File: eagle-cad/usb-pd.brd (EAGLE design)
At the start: 100 x 80 mm, 24 parts, among them Q1 CERAMIC_RESONATOR_SMD6M00G53Z, U1 ATMEGA328-AU

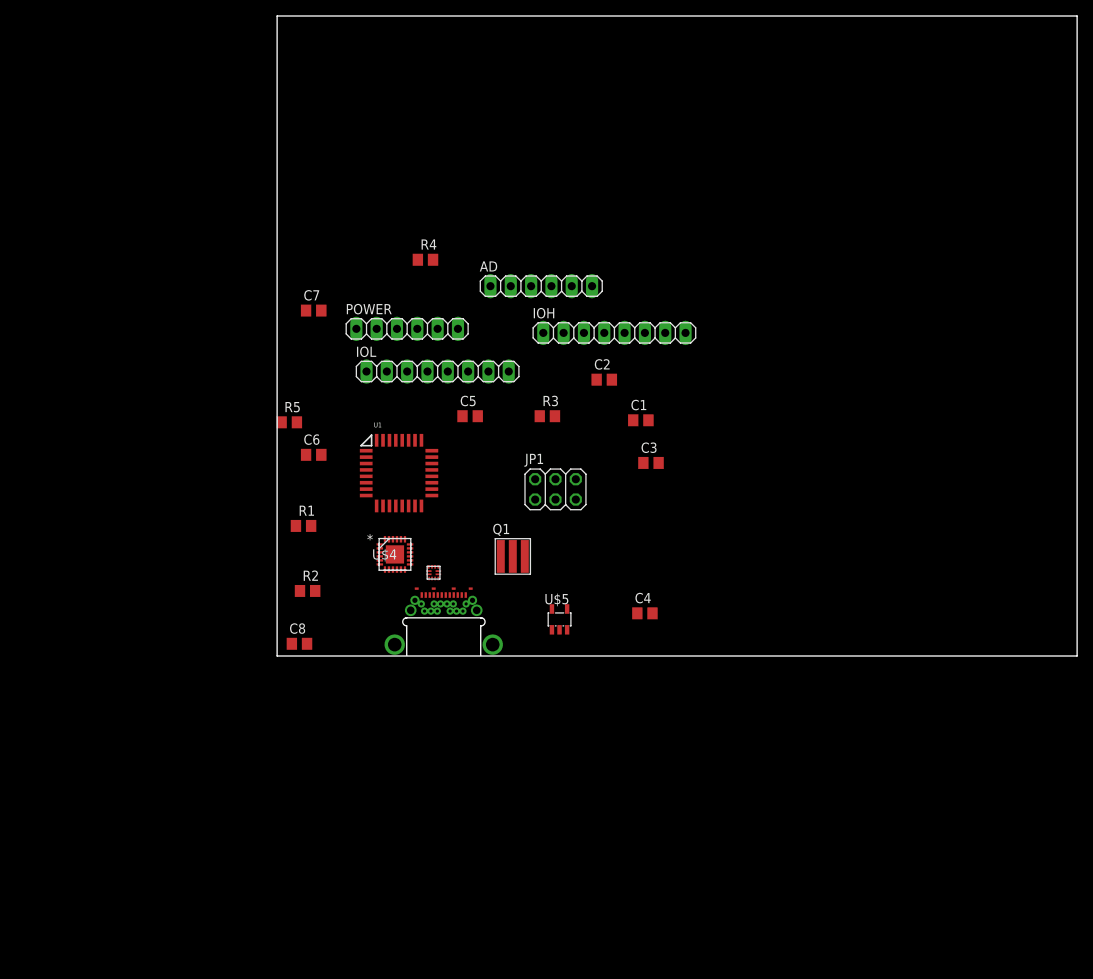
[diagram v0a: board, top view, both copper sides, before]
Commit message: Filled out PTN5150, arranged board like an Uno rev3
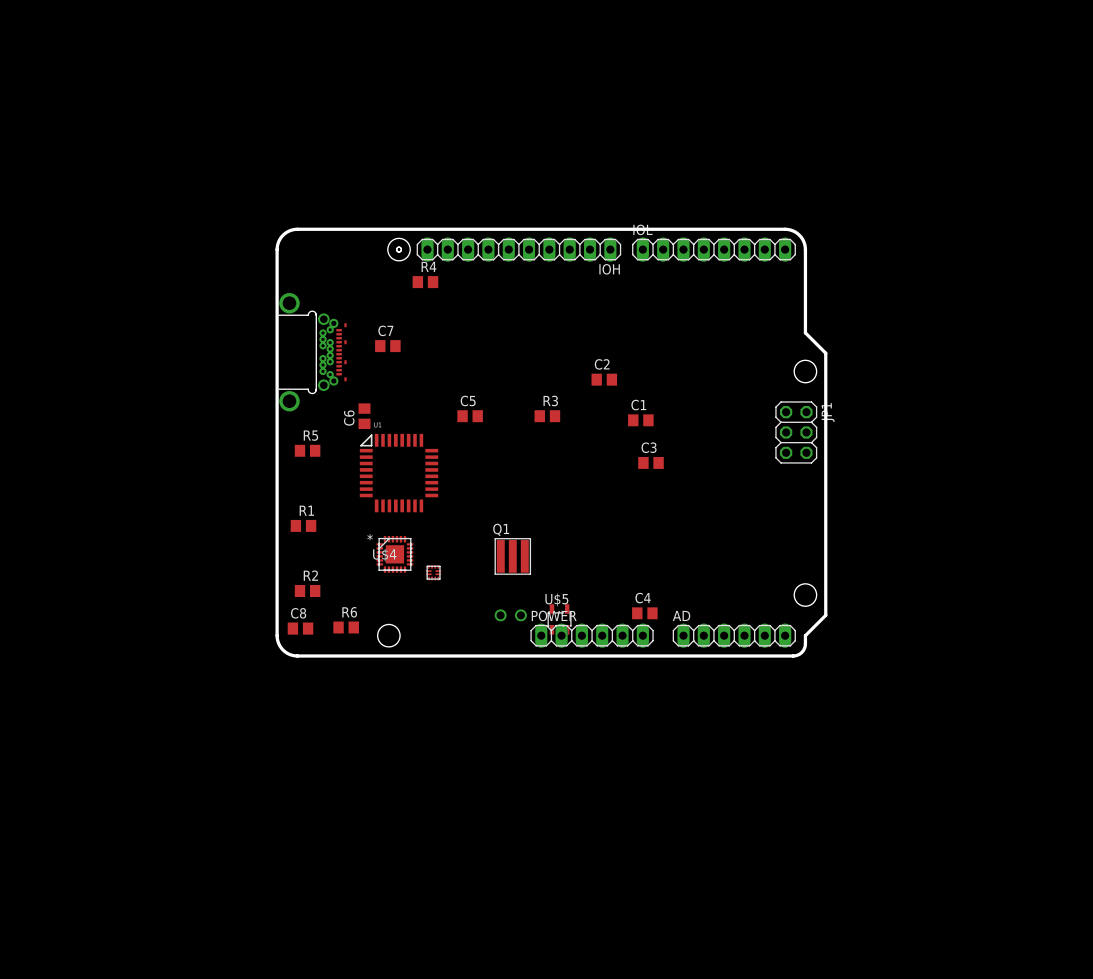
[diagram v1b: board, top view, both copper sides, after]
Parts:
- added R6: 10k, rcl:R0805
- IOH: device pinhead:1X08 -> pinhead:1X10
- R3: value (none) -> 10k
- moved AD 49.9 mm to (57.1, 2.54)
- moved POWER 44.8 mm to (39.4, 2.54)
- moved IOL 37.8 mm to (54.6, 50.8)
- moved U$1 33.1 mm to (7.75, 38.0), turned to 270 degrees
- moved JP1 30.9 mm to (64.9, 27.9), turned to 270 degrees
- moved IOH 15.8 mm to (30.2, 50.8), turned to 180 degrees
- moved C7 10.3 mm to (13.8, 38.7)
- moved C6 7.98 mm to (10.9, 30.0), turned to 90 degrees
- moved R5 4.23 mm to (3.81, 25.7)
- moved R4 2.79 mm to (18.5, 46.7)
- moved C8 1.91 mm to (2.92, 3.43)
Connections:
- new net N$8: R6.1, U$3.P$5
- net +5V: now also R6.2, U$3.P$12
- net GND: now also U$1.A$1, U$1.A$12, U$1.B$1, U$1.B$12, U$3.P$10, U$3.P$11, U$3.P$3
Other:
- board size 100 x 80 mm -> 68.6 x 53.3 mm

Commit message: Added 5V buck implementation (need power FET to control it)
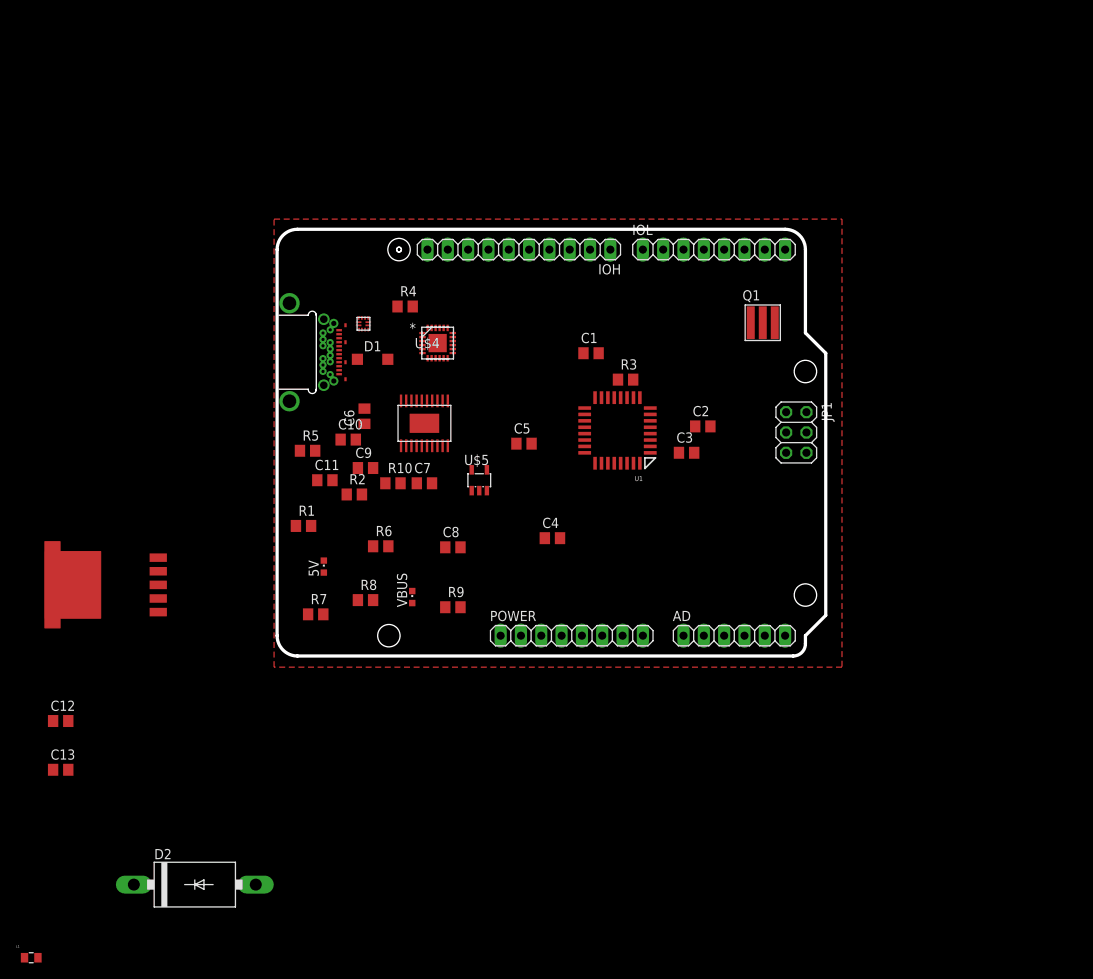
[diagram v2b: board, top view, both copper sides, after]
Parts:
- added 5V, VBUS: (no value), led:CHIPLED_0603
- added C10, C11: 47uF, rcl:C0805
- added C12: 100uF, rcl:C0805
- added C13: 1mF, rcl:C0805
- added C9: (no value), rcl:C0805
- added D1: MBR0520LT, diode:SOD123
- added D2: 1N5822, diode:DO201-15
- added L1: (no value), EagleLibrary_Wuerth_Elektronik_eiSos_rev16a:WE-RFI_0805
- added R10: 10k, rcl:R0805
- added R7: 300, rcl:R0805
- added R8, R9: 1.5k, rcl:R0805
- added U$2: TI-TPS7B6750-Q1, usb-pd:HTSSOP-20
- added U$6: TI-LM2576-5.0, usb-pd:TO-263
- POWER: device pinhead:1X06 -> pinhead:1X08
- moved Q1 42.8 mm to (60.7, 41.7)
- moved U$3 32.3 mm to (10.8, 41.5)
- moved U1 27.8 mm to (42.5, 28.2), turned to 180 degrees
- moved U$4 26.9 mm to (20.1, 39.1)
- moved C8 21.6 mm to (22.0, 13.6)
- moved U$5 20.1 mm to (25.3, 22.0)
- moved C7 17.7 mm to (18.4, 21.6)
- moved C4 14.9 mm to (34.4, 14.7)
- moved C2 13.6 mm to (53.2, 28.7)
- moved R2 13.4 mm to (9.65, 20.2)
- moved R6 11.0 mm to (13.0, 13.7)
- moved R3 10.8 mm to (43.6, 34.5)
- moved C1 10.4 mm to (39.2, 37.8)
- moved C5 7.55 mm to (30.9, 26.5)
- moved C3 4.62 mm to (51.2, 25.4)
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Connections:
- removed net IO0: IOL.1, U1.P$30
- removed net IO1: IOL.2, U1.P$31
- new net N$1: C12.1, U$6.P$1
- new net N$10: 5V.A, R7.1
- new net N$11: R9.1, VBUS.A
- new net N$12: R8.1, R9.2
- new net N$13: R10.1, U$2.P$1
- new net N$14: C9.1, U$2.P$3
- new net N$15: C13.1, L1.2, U$6.P$4
- new net N$40: C10.1, D1.C, R8.2, U$2.P$15, U$2.P$19
- new net N$9: D2.C, L1.1, U$6.P$2
- net +3V3: now also POWER.4
- net +5V: now also C11.1, POWER.5, R10.2, R7.2, U$2.P$4
- net GND: now also 5V.C, C10.2, C11.2, C13.2, C9.2, D2.A, POWER.6, POWER.7, U$2.P$13, U$2.P$8, U$6.P$3, U$6.P$5, U$6.P$6, VBUS.C
- net RESET: now also POWER.3
- net USB_RX: now also IOL.1, U1.P$30
- net USB_TX: now also IOL.2, U1.P$31
- net VBUS: now also D1.A, POWER.8
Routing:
- added copper zone on layer 1, net GND

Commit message: Added a n-channel power MOSFET to serve as controlling power FET for 5V buck. Definitely needs review
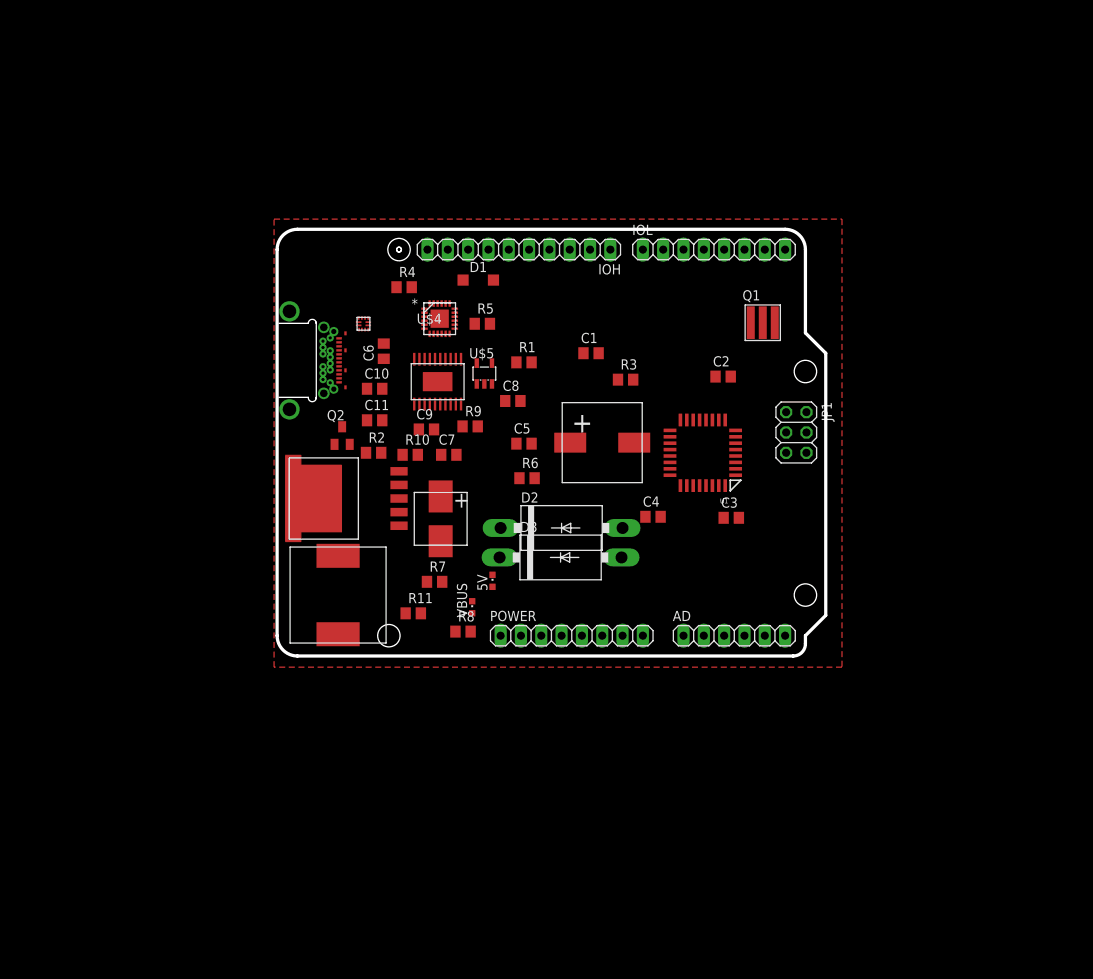
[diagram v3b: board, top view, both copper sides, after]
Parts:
- removed C12: 100uF, rcl:C0805
- removed L1: (no value), EagleLibrary_Wuerth_Elektronik_eiSos_rev16a:WE-RFI_0805
- added D3: 1N5822, diode:DO201-15
- added Q2: NDS351N, transistor-small-signal:SOT23
- added R11: 10k, rcl:R0805
- added U$7: WEURTH-784771101, usb-pd:1260
- added U$8: UWT1V101MCL1GS, usb-pd:UWT1V101MCL1GS
- C13: value 1mF -> AVE108M10G24T-F; device rcl:C0805 -> usb-pd:AVE108M10G
- moved C13 79.1 mm to (40.6, 26.7)
- moved D2 63.9 mm to (35.6, 16.0)
- moved R1 34.3 mm to (30.9, 36.7)
- moved U$6 32.0 mm to (15.2, 19.7)
- moved R5 27.0 mm to (25.7, 41.5)
- moved R9 22.7 mm to (24.1, 28.7)
- moved 5V 21.2 mm to (26.9, 9.40)
- moved R6 20.2 mm to (31.2, 22.2)
- moved C8 19.8 mm to (29.5, 31.9)
- moved D1 16.5 mm to (25.1, 47.0)
- moved R7 15.4 mm to (19.7, 9.27)
- moved U$5 13.4 mm to (25.9, 35.3)
- moved C4 12.9 mm to (47.0, 17.4)
- moved R8 12.8 mm to (23.2, 3.05)
- moved U1 11.0 mm to (53.2, 25.4)
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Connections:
- net +5V: now also D3.C, R11.2
- net GND: now also C13.P$2, U$8.P$2; no longer C13.2
- net IO2: now also Q2.1, R11.1
- net N$1: now also Q2.2, U$8.P$1; no longer C12.1
- net N$15: now also C13.P$1, D3.A, U$7.P$2; no longer C13.1, L1.2
- net N$9: now also U$7.P$1; no longer L1.1
- net VBUS: now also Q2.3
